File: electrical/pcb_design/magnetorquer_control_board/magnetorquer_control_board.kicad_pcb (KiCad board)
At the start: 4 copper layers, 77 x 96 mm, 70 parts, among them J1 STLINK, J2 STLINK, J3 Molex_504050-1291, J4 External Power, J5 Molex_504050-1291, J6 Molex_504050-0891, J7 Molex_504050-0891, J8 Molex_504050-0491, U1 STM32L452RCT6, U2 BMI323, U3 BMI323, U4 TCAN330DR, U5 INA260, U6 TLV76733DRVx

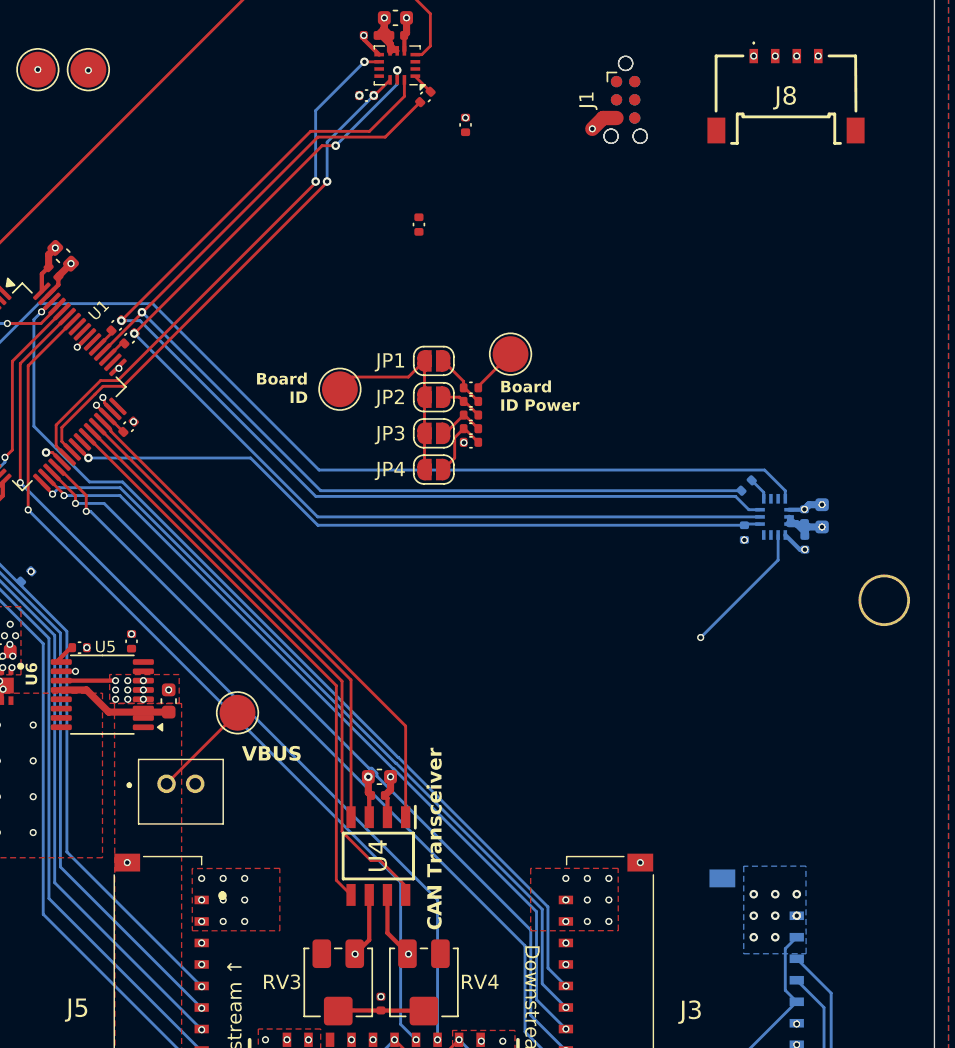
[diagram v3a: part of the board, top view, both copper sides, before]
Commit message: Stitch around long traces that were creating disconnects in the +3V3 net.
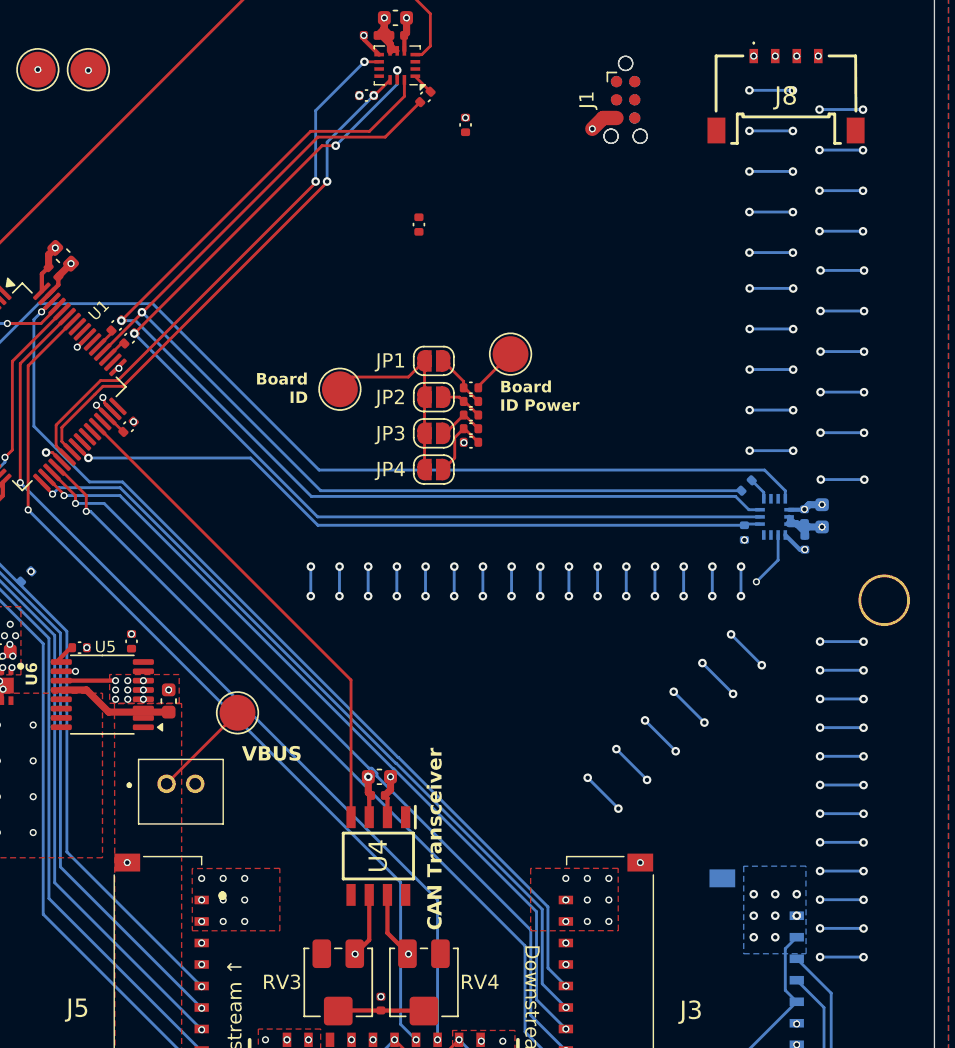
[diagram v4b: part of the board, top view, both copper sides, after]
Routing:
- net +3V3: track 24.8 -> 157.5 mm, vias 27 -> 125
- net CAN1_SILENT: track 41.1 -> 0.00 mm
- net CAN1_SHUTDOWN: track 39.6 -> 0.00 mm
- net CAN1_TX: track 36.3 -> 0.00 mm
- net VCC: track 4.23 -> 19.4 mm, vias 38 -> 48
- net IMU2_INT2: track 61.8 -> 58.6 mm

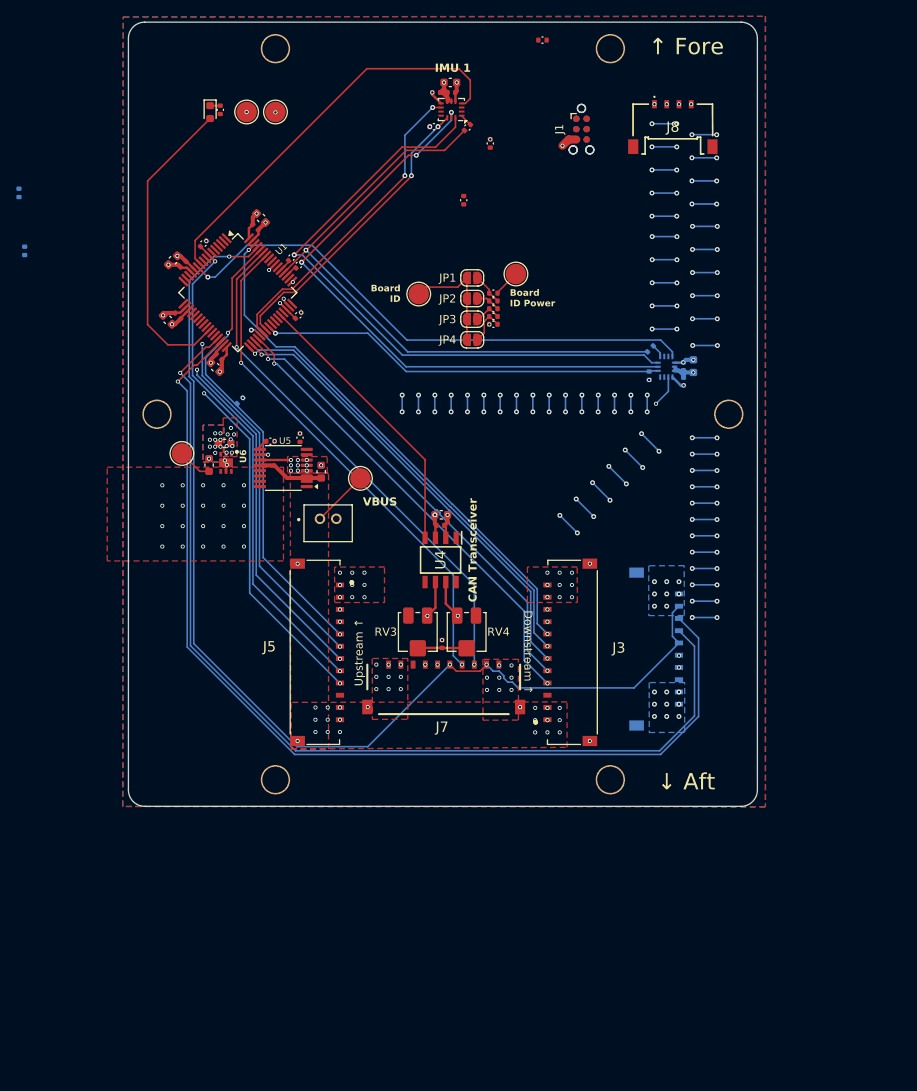
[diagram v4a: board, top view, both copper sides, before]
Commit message: Finish routing all traces. Some parts (mostly resistors) still unchosen. Need to audit for JLCPCB Basic vs Extended components to manage cost.
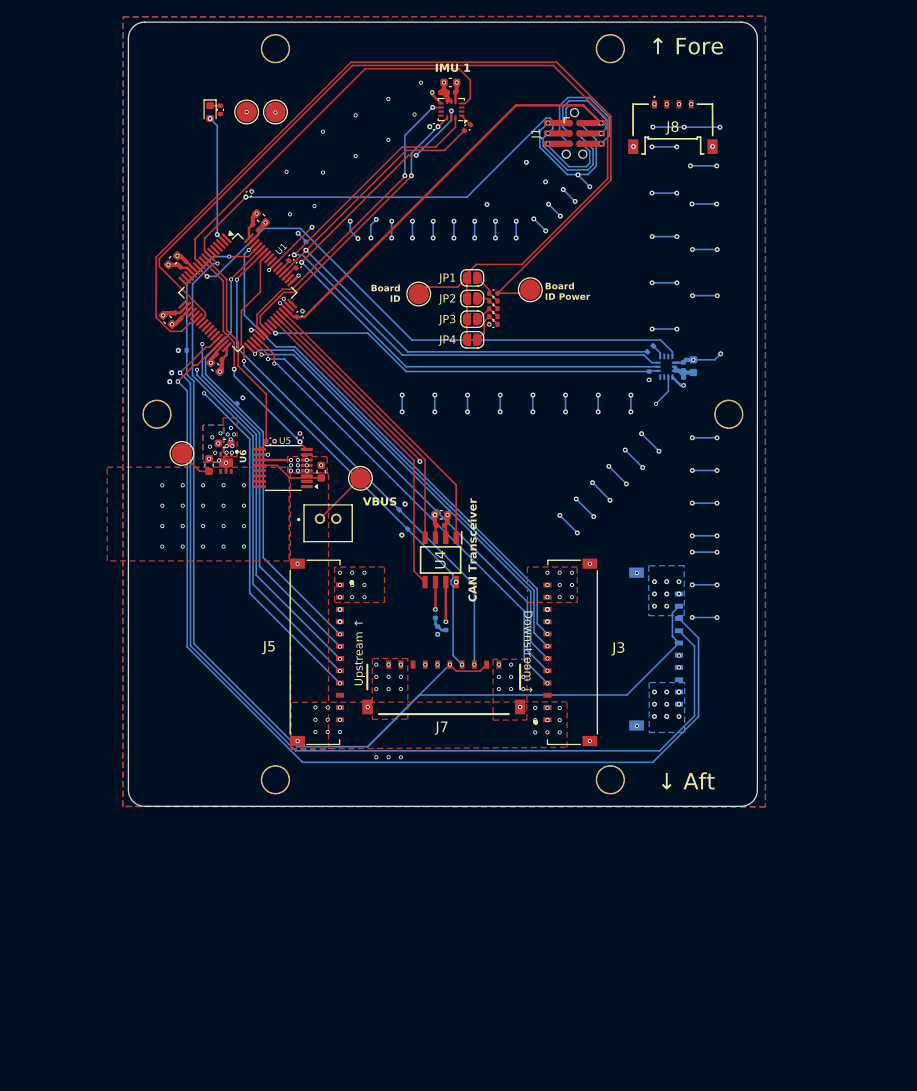
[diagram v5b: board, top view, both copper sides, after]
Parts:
- removed J2: STLINK, Connector:Tag-Connect_TC2030-IDC-NL_2x03_P1.27mm_Vertical
- added R23: 7.5k-10k, footprints:Nondescript_R_0402_1005Metric, B.Cu at (122.1, 90.3)
- C1, R1, R22, R4: moved to B.Cu
- J1: footprint Connector:Tag-Connect_TC2030-IDC-NL_2x03_P1.27mm_Vertical -> footprints:Double-Sided_Tag-Connect_TC2030-IDC-NL_2x03_P1.27mm_Vertical
- RV3, RV4: value R200 -> ~60; footprint Potentiometer_SMD:Potentiometer_Bourns_3314J_Vertical -> footprints:Nondescript_R_0402_1005Metric; moved to B.Cu
- moved R1 45.8 mm to (149.0, 109.5), turned to -135 degrees
- moved R4 41.2 mm to (149.3, 112.6), turned to 45 degrees
- moved R22 38.4 mm to (137.2, 77.5), turned to -90 degrees
- moved R2 29.9 mm to (121.0, 94.1), turned to 0 degrees
- moved R5 23.8 mm to (121.3, 93.0), turned to 0 degrees
- moved R8 8.22 mm to (130.2, 71.2)
- moved RV3 3.11 mm to (153.0, 122.6), turned to 90 degrees
- moved RV4 2.65 mm to (154.3, 124.1), turned to -90 degrees
- moved TP7 2.61 mm to (164.6, 82.9)
- moved C1 1.74 mm to (153.3, 124.6), turned to 90 degrees
- moved J1 1.00 mm to (170.1, 63.8)
- moved R7 0.23 mm to (136.4, 85.9)
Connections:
- RV3 pad 1: unconnected-(RV3-Pad1) -> Net-(C1-Pad2)
- RV3 pad 2: Net-(C1-Pad2) -> CANL
- U1 pad 2: unconnected-(U1-PC13-Pad2) -> /DEBUG_LED
- U1 pad 26: /DEBUG_LED -> unconnected-(U1-PB0-Pad26)
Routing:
- net BOARD_ID_PWR: track 3.18 -> 113.7 mm
- net BOARD_ID_SENS: track 14.3 -> 121.7 mm
- net NRST: track 61.3 -> 127.2 mm, vias 2 -> 3
- net TRACESWO: track 57.5 -> 121.0 mm, vias 3 -> 4
- net SWCLK: track 58.8 -> 120.7 mm
- net SWDIO: track 60.7 -> 119.4 mm
- net CAN1_SILENT: track 0.00 -> 41.3 mm, vias 0 -> 2
- net CAN1_SHUTDOWN: track 0.00 -> 39.6 mm
- net CAN1_TX: track 0.00 -> 36.3 mm
- net I2C3_SDA: track 0.00 -> 28.3 mm, vias 0 -> 2
- net I2C3_SCL: track 1.41 -> 26.7 mm
- net /DEBUG_LED: track 37.7 -> 15.7 mm, vias 0 -> 2
- net VCC: track 19.4 -> 38.4 mm, vias 48 -> 47
- net NMAG_FAULT: track 132.9 -> 149.4 mm, vias 3 -> 2
- net GND: track 36.4 -> 44.1 mm, vias 75 -> 87
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
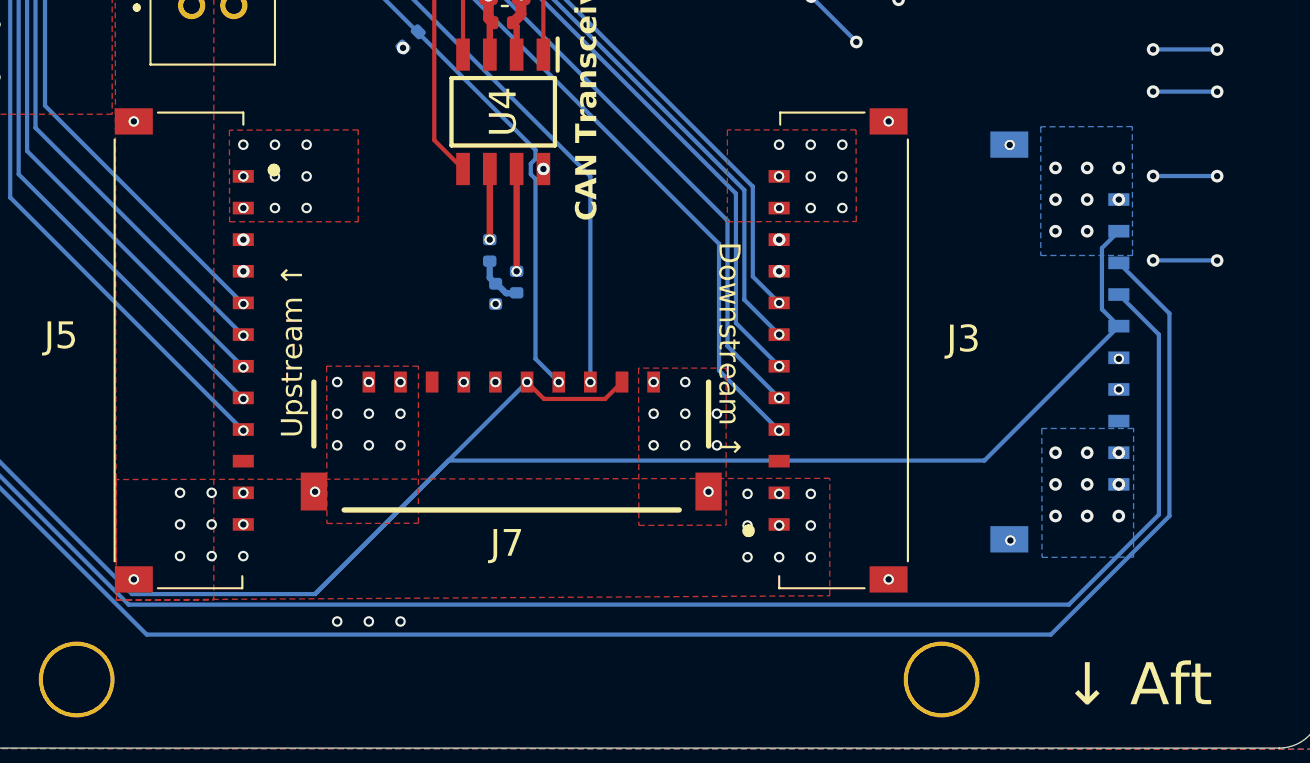
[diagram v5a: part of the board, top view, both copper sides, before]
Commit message: Move the magnetorquer header for the adjacent magnetorquer board close enough so that a 50mm cable can be used, rather than a 100mm cable.
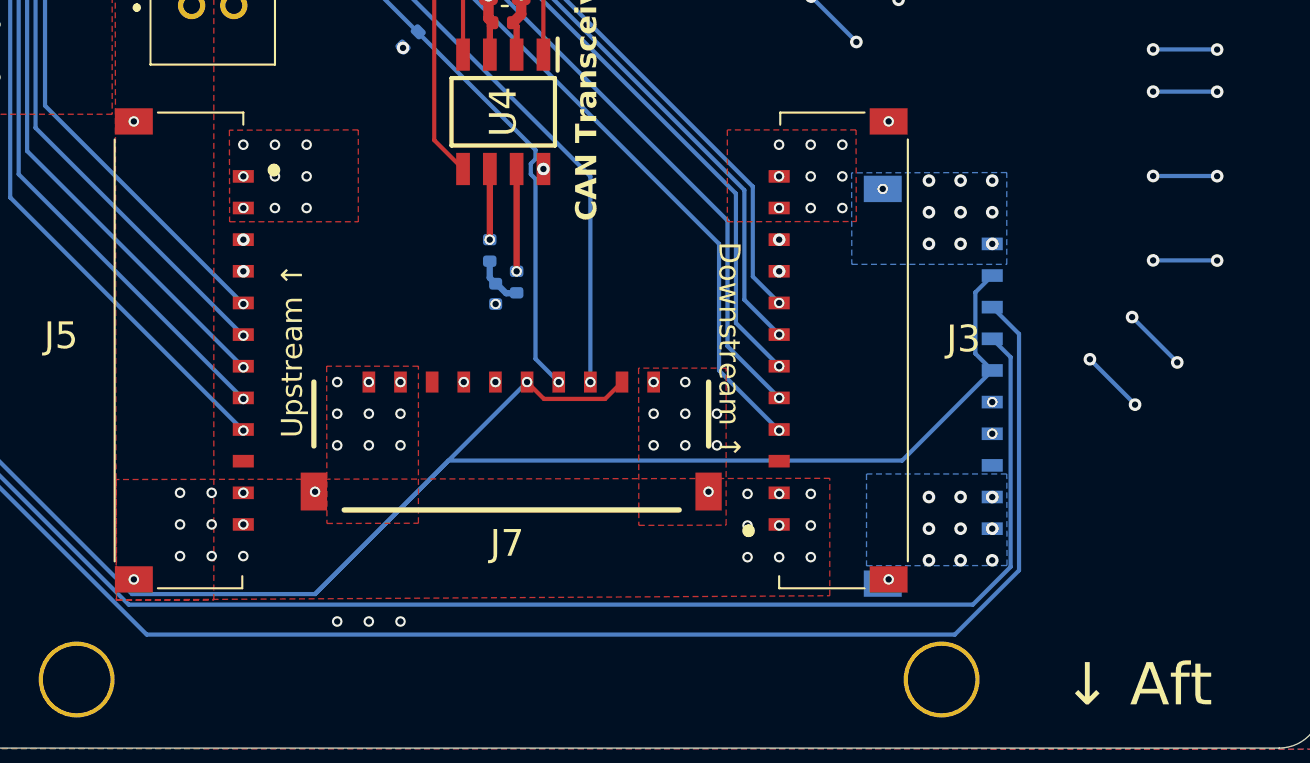
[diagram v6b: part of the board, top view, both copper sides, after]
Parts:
- moved J6 6.36 mm to (176.8, 135.8)
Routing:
- net I2C2_SDA: track 124.1 -> 115.9 mm
- net I2C2_SCL: track 120.3 -> 112.2 mm
- net /Magnetorquer Control/VSOLAR_1_1: track 71.2 -> 78.0 mm
- net NMAG_FAULT: track 149.4 -> 142.5 mm
- net /Magnetorquer Control/VSOLAR_1_2: track 69.9 -> 76.8 mm
- net VCC: track 38.4 -> 44.4 mm, vias 47 -> 51

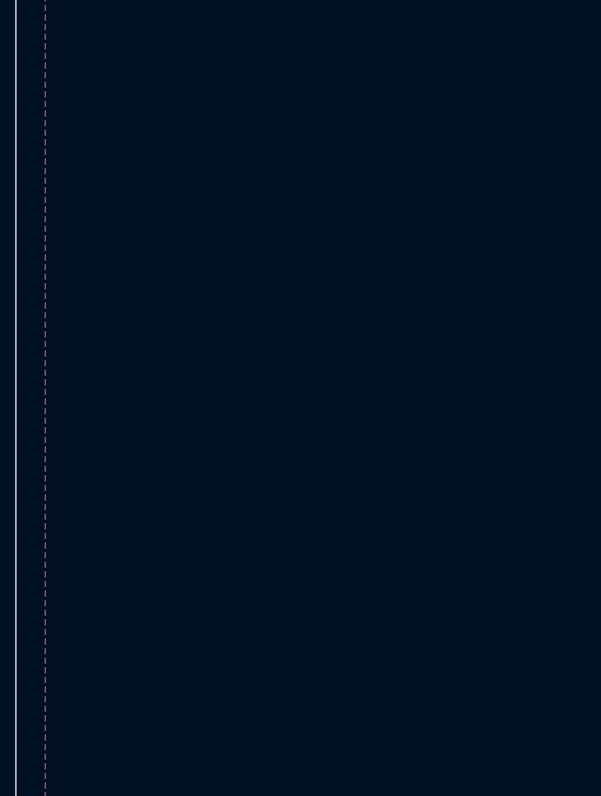
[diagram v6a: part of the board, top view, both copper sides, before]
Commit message: Pick specific resistor values and part numbers for most of the resistors in the magnetorquer control board. This change also includes selecting resistors to match the CanonicalBoardIds in //hal/board_identification.
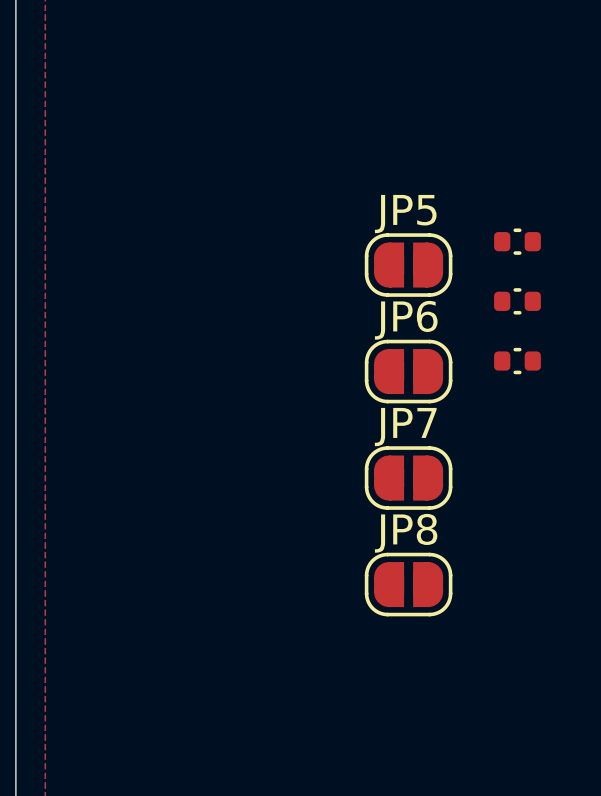
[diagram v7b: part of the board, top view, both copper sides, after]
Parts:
- added JP5: SolderJumper_2_Open, Jumper:SolderJumper-2_P1.3mm_Open_RoundedPad1.0x1.5mm, F.Cu at (205.5, 78.3)
- added JP6: SolderJumper_2_Open, Jumper:SolderJumper-2_P1.3mm_Open_RoundedPad1.0x1.5mm, F.Cu at (205.5, 81.8)
- added JP7: SolderJumper_2_Open, Jumper:SolderJumper-2_P1.3mm_Open_RoundedPad1.0x1.5mm, F.Cu at (205.5, 85.4)
- added JP8: SolderJumper_2_Open, Jumper:SolderJumper-2_P1.3mm_Open_RoundedPad1.0x1.5mm, F.Cu at (205.5, 88.9)
- added R24: 15k8, footprints:Nondescript_R_0402_1005Metric, F.Cu at (209.2, 77.5)
- added R25: 9k31, footprints:Nondescript_R_0402_1005Metric, F.Cu at (209.2, 79.5)
- added R26: 15k8, footprints:Nondescript_R_0402_1005Metric, F.Cu at (209.2, 81.5)
- R1, R16, R17, R2, R22, R23, R3, R4, R5, R6: value 7.5k-10k -> 9k31
- R11, R14: value R -> 18k7
- R12, R13: value R -> 6k19
- R15: value R -> 9k31
- RV3, RV4: value ~60 -> 60
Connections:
- R11 pad 1: BOARD_ID_PWR -> Net-(JP5-B)
- R12 pad 2: Net-(JP2-B) -> GND
- R13 pad 1: Net-(JP2-B) -> Net-(JP6-B)
- R13 pad 2: Net-(JP3-B) -> Net-(JP2-B)
- R14 pad 1: Net-(JP3-B) -> Net-(JP2-B)
- R14 pad 2: Net-(JP4-B) -> GND
- R15 pad 1: GND -> Net-(JP3-B)
- R15 pad 2: Net-(JP4-B) -> Net-(JP7-B)
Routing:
- net Net-(JP3-B): vias 0 -> 1
- net GND: vias 87 -> 86
